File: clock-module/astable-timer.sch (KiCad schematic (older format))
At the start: 8 parts

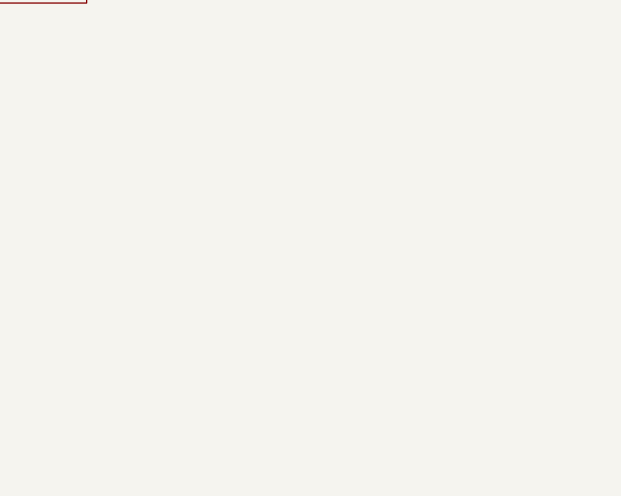
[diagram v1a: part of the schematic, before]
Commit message: Add LED to all outputs of clocl-module
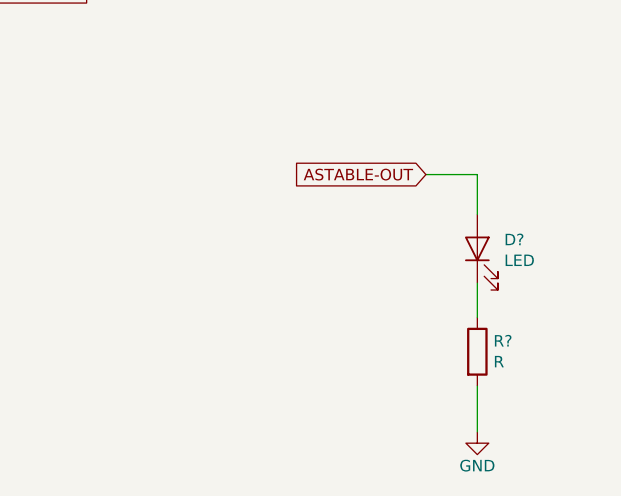
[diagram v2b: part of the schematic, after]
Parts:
- added D?: LED, symbol Device:LED
- added R?: R, symbol Device:R
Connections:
- net ASTABLE-OUT: now also D?.2 (A)
- net GND: now also R?.2
- new net: D?.1 (K), R?.1
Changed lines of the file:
@@
 Text GLabel 4900 3250 2    50   Input ~ 0
 ASTABLE-OUT
+Text GLabel 6950 4050 0    50   Input ~ 0
+ASTABLE-OUT
+$Comp
+L Device:LED D?
+U 1 1 5D29BC02
+P 7175 4375
+F 0 "D?" V 7214 4258 50  0000 R CNN
+F 1 "LED" V 7123 4258 50  0000 R CNN
+F 2 "" H 7175 4375 50  0001 C CNN
+F 3 "~" H 7175 4375 50  0001 C CNN
+	1    7175 4375
+	0    -1   -1   0
+$EndComp
+$Comp
+L power:GND #PWR?
+U 1 1 5D29D018
+P 7175 5175
+F 0 "#PWR?" H 7175 4925 50  0001 C CNN
+F 1 "GND" H 7175 5025 50  0000 C CNN
+F 2 "" H 7175 5175 50  0001 C CNN
+F 3 "" H 7175 5175 50  0001 C CNN
+	1    7175 5175
+	1    0    0    -1
+$EndComp
+Wire Wire Line
+	6950 4050 7175 4050
+Wire Wire Line
+	7175 4050 7175 4225
+Wire Wire Line
+	7175 4525 7175 4675
+$Comp
+L Device:R R?
+U 1 1 5D2B5766
+P 7175 4825
+F 0 "R?" H 7245 4871 50  0000 L CNN
+F 1 "R" H 7245 4780 50  0000 L CNN
+F 2 "" V 7105 4825 50  0001 C CNN
+F 3 "~" H 7175 4825 50  0001 C CNN
+	1    7175 4825
+	1    0    0    -1
+$EndComp
+Wire Wire Line
+	7175 5175 7175 4975
 $EndSCHEMATC

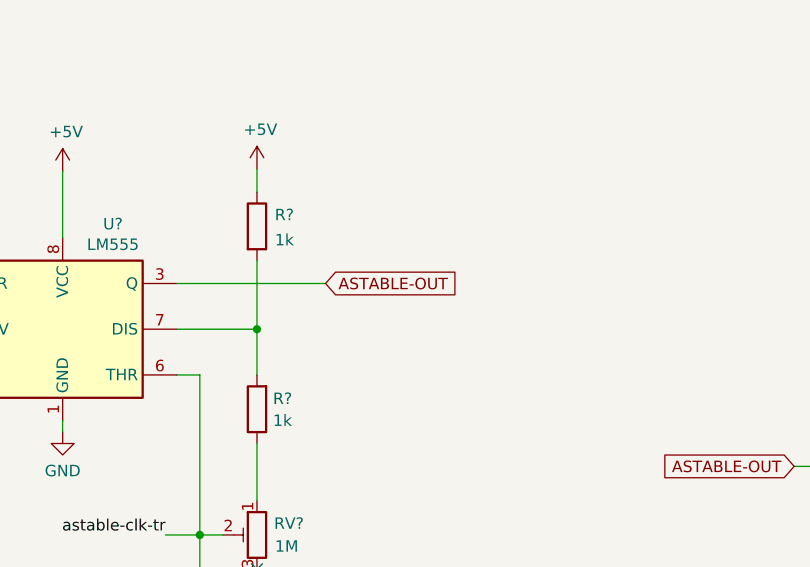
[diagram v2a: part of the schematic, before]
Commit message: Add clock inverter to clock-module, correct label directions
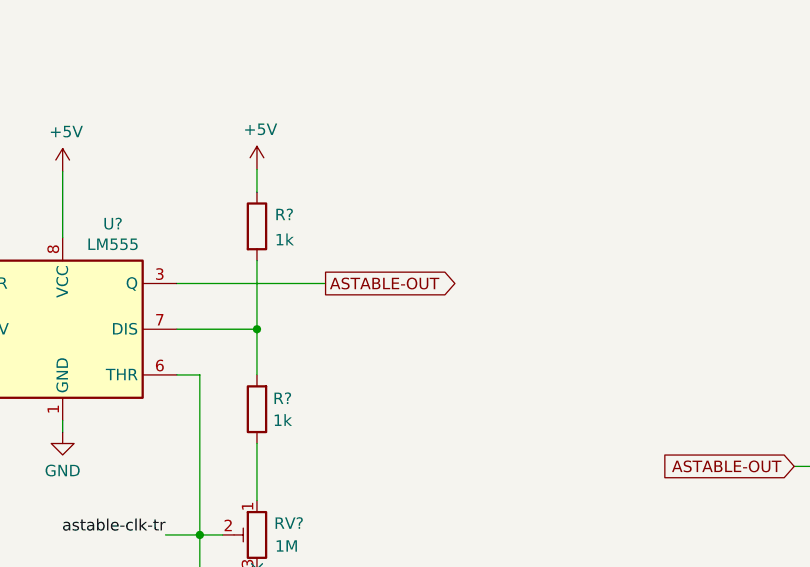
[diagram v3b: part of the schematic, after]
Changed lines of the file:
@@
 	0    -1   -1   0
 $EndComp
-Text GLabel 4900 3250 2    50   Input ~ 0
+Text GLabel 4900 3250 2    50   Output ~ 0
 ASTABLE-OUT
 Text GLabel 6950 4050 0    50   Input ~ 0

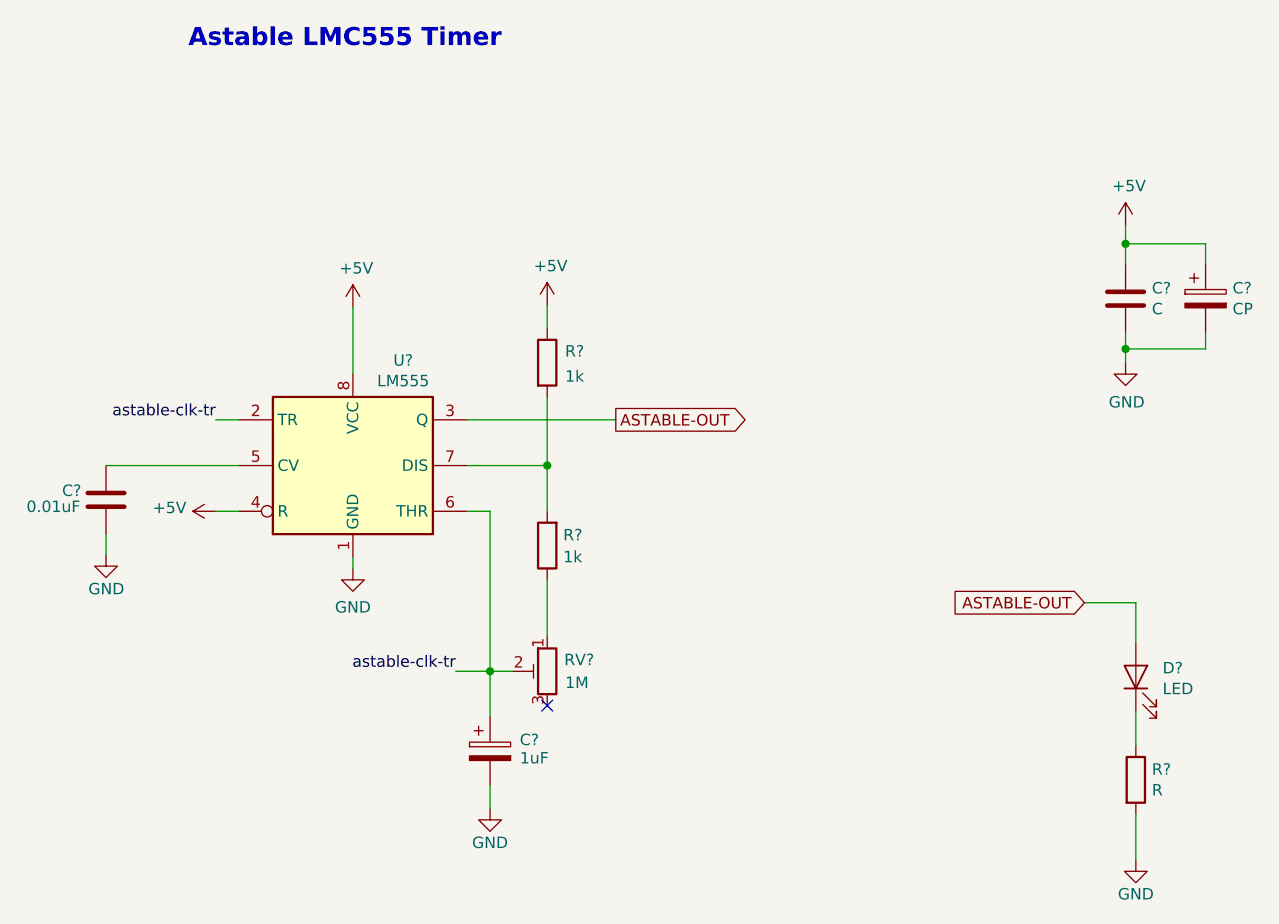
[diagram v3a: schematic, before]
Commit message: ERC complete on clock-module, add HLT connector
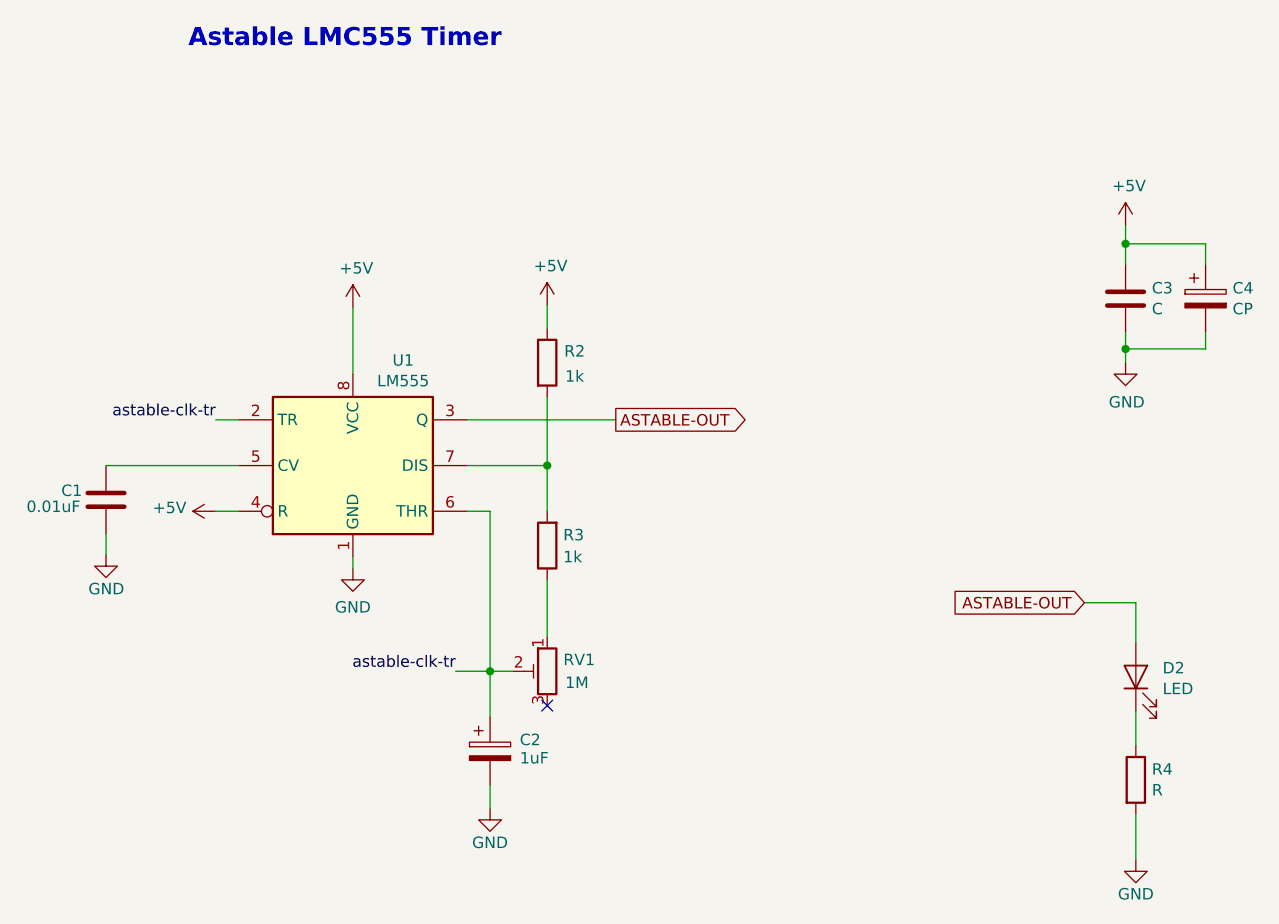
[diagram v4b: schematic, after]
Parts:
- gave numbers to parts that had none: 10
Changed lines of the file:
@@
 $EndDescr
 $Comp
-L Timer:LM555 U?
+L Timer:LM555 U1
 U 1 1 5D272A60
 P 3750 3450
-F 0 "U?" H 3970 3910 50  0000 C CNN
+F 0 "U1" H 3970 3910 50  0000 C CNN
 F 1 "LM555" H 3970 3820 50  0000 C CNN
 F 2 "" H 3750 3450 50  0001 C CNN
@@
 $EndComp
 $Comp
-L Device:R R?
+L Device:R R2
 U 1 1 5D272A66
 P 4600 3000
-F 0 "R?" H 4720 3050 50  0000 C CNN
+F 0 "R2" H 4720 3050 50  0000 C CNN
 F 1 "1k" H 4720 2940 50  0000 C CNN
 F 2 "" V 4530 3000 50  0001 C CNN
@@
 $EndComp
 $Comp
-L Device:R R?
+L Device:R R3
 U 1 1 5D272A6C
 P 4600 3800
-F 0 "R?" H 4530 3754 50  0000 R CNN
+F 0 "R3" H 4530 3754 50  0000 R CNN
 F 1 "1k" H 4530 3850 50  0000 R CNN
 F 2 "" V 4530 3800 50  0001 C CNN
@@
 $EndComp
 $Comp
-L Device:R_POT_TRIM RV?
+L Device:R_POT_TRIM RV1
 U 1 1 5D272A72
 P 4600 4350
-F 0 "RV?" H 4460 4400 50  0000 C CNN
+F 0 "RV1" H 4460 4400 50  0000 C CNN
 F 1 "1M" H 4470 4300 50  0000 C CNN
 F 2 "" H 4600 4350 50  0001 C CNN
@@
 P 2670 3600
 AR Path="/5D272A78" Ref="C?"  Part="1"
-AR Path="/5D26EDA1/5D272A78" Ref="C?"  Part="1"
-F 0 "C?" H 2520 3640 50  0000 C CNN
+AR Path="/5D26EDA1/5D272A78" Ref="C1"  Part="1"
+F 0 "C1" H 2520 3640 50  0000 C CNN
 F 1 "0.01uF" H 2440 3570 50  0000 C CNN
 F 2 "" H 2708 3450 50  0001 C CNN
@@
 $EndComp
 $Comp
-L Device:CP C?
+L Device:CP C2
 U 1 1 5D272A7E
 P 4350 4700
-F 0 "C?" H 4480 4750 50  0000 L CNN
+F 0 "C2" H 4480 4750 50  0000 L CNN
 F 1 "1uF" H 4480 4670 50  0000 L CNN
 F 2 "" H 4388 4550 50  0001 C CNN
@@
 P 2670 3840
 AR Path="/5D272A9B" Ref="#PWR?"  Part="1"
-AR Path="/5D26EDA1/5D272A9B" Ref="#PWR?"  Part="1"
-F 0 "#PWR?" H 2670 3590 50  0001 C CNN
+AR Path="/5D26EDA1/5D272A9B" Ref="#PWR0108"  Part="1"
+F 0 "#PWR0108" H 2670 3590 50  0001 C CNN
 F 1 "GND" H 2750 3690 50  0000 R CNN
 F 2 "" H 2670 3840 50  0001 C CNN
@@
 $EndComp
 $Comp
-L power:GND #PWR?
+L power:GND #PWR0109
 U 1 1 5D272AA1
 P 3750 3900
-F 0 "#PWR?" H 3750 3650 50  0001 C CNN
+F 0 "#PWR0109" H 3750 3650 50  0001 C CNN
 F 1 "GND" H 3750 3730 50  0000 C CNN
 F 2 "" H 3750 3900 50  0001 C CNN
@@
 	4350 4350 4200 4350
 $Comp
-L power:GND #PWR?
+L power:GND #PWR0110
 U 1 1 5D272AB3
 P 4350 4950
-F 0 "#PWR?" H 4350 4700 50  0001 C CNN
+F 0 "#PWR0110" H 4350 4700 50  0001 C CNN
 F 1 "GND" H 4350 4800 50  0000 C CNN
 F 2 "" H 4350 4950 50  0001 C CNN
@@
 P 7130 2720
 AR Path="/5D274115" Ref="C?"  Part="1"
-AR Path="/5D26EDA1/5D274115" Ref="C?"  Part="1"
-F 0 "C?" H 7245 2766 50  0000 L CNN
+AR Path="/5D26EDA1/5D274115" Ref="C3"  Part="1"
+F 0 "C3" H 7245 2766 50  0000 L CNN
 F 1 "C" H 7245 2675 50  0000 L CNN
 F 2 "" H 7168 2570 50  0001 C CNN
@@
 P 7480 2720
 AR Path="/5D27411B" Ref="C?"  Part="1"
-AR Path="/5D26EDA1/5D27411B" Ref="C?"  Part="1"
-F 0 "C?" H 7598 2766 50  0000 L CNN
+AR Path="/5D26EDA1/5D27411B" Ref="C4"  Part="1"
+F 0 "C4" H 7598 2766 50  0000 L CNN
 F 1 "CP" H 7598 2675 50  0000 L CNN
 F 2 "" H 7518 2570 50  0001 C CNN
@@
 P 7130 3000
 AR Path="/5D27412C" Ref="#PWR?"  Part="1"
-AR Path="/5D26EDA1/5D27412C" Ref="#PWR?"  Part="1"
-F 0 "#PWR?" H 7130 2750 50  0001 C CNN
+AR Path="/5D26EDA1/5D27412C" Ref="#PWR0111"  Part="1"
+F 0 "#PWR0111" H 7130 2750 50  0001 C CNN
 F 1 "GND" H 7135 2827 50  0000 C CNN
 F 2 "" H 7130 3000 50  0001 C CNN
@@
 Astable LMC555 Timer
 $Comp
-L power:+5V #PWR?
+L power:+5V #PWR0112
 U 1 1 5D282537
 P 3750 2760
-F 0 "#PWR?" H 3750 2610 50  0001 C CNN
+F 0 "#PWR0112" H 3750 2610 50  0001 C CNN
 F 1 "+5V" H 3765 2933 50  0000 C CNN
 F 2 "" H 3750 2760 50  0001 C CNN
@@
 $EndComp
 $Comp
-L power:+5V #PWR?
+L power:+5V #PWR0113
 U 1 1 5D282E9F
 P 4600 2750
-F 0 "#PWR?" H 4600 2600 50  0001 C CNN
+F 0 "#PWR0113" H 4600 2600 50  0001 C CNN
 F 1 "+5V" H 4615 2923 50  0000 C CNN
 F 2 "" H 4600 2750 50  0001 C CNN
@@
 $EndComp
 $Comp
-L power:+5V #PWR?
+L power:+5V #PWR0114
 U 1 1 5D2835DA
 P 7130 2400
-F 0 "#PWR?" H 7130 2250 50  0001 C CNN
+F 0 "#PWR0114" H 7130 2250 50  0001 C CNN
 F 1 "+5V" H 7145 2573 50  0000 C CNN
 F 2 "" H 7130 2400 50  0001 C CNN
@@
 $EndComp
 $Comp
-L power:+5V #PWR?
+L power:+5V #PWR0115
 U 1 1 5D283E2C
 P 3150 3650
-F 0 "#PWR?" H 3150 3500 50  0001 C CNN
+F 0 "#PWR0115" H 3150 3500 50  0001 C CNN
 F 1 "+5V" V 3165 3778 50  0000 L CNN
 F 2 "" H 3150 3650 50  0001 C CNN
@@
 ASTABLE-OUT
 $Comp
-L Device:LED D?
+L Device:LED D2
 U 1 1 5D29BC02
 P 7175 4375
-F 0 "D?" V 7214 4258 50  0000 R CNN
+F 0 "D2" V 7214 4258 50  0000 R CNN
 F 1 "LED" V 7123 4258 50  0000 R CNN
 F 2 "" H 7175 4375 50  0001 C CNN
@@
 $EndComp
 $Comp
-L power:GND #PWR?
+L power:GND #PWR0116
 U 1 1 5D29D018
 P 7175 5175
-F 0 "#PWR?" H 7175 4925 50  0001 C CNN
+F 0 "#PWR0116" H 7175 4925 50  0001 C CNN
 F 1 "GND" H 7175 5025 50  0000 C CNN
 F 2 "" H 7175 5175 50  0001 C CNN
@@
 	7175 4525 7175 4675
 $Comp
-L Device:R R?
+L Device:R R4
 U 1 1 5D2B5766
 P 7175 4825
-F 0 "R?" H 7245 4871 50  0000 L CNN
+F 0 "R4" H 7245 4871 50  0000 L CNN
 F 1 "R" H 7245 4780 50  0000 L CNN
 F 2 "" V 7105 4825 50  0001 C CNN
